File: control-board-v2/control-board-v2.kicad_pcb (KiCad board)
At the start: 2 copper layers, 90 x 50 mm, 134 parts, among them J1 Conn_01x03, J12 Conn_01x01_Pin, J13 Conn_01x01_Pin, J14 Conn_01x02, J15 Conn_01x01_Pin, J16 Conn_01x02, J17 Conn_01x02, J18 Conn_01x02, J19 Conn_01x01_Pin, J2 GPS_ANT, J20 Conn_01x01_Pin, J21 Conn_01x01_Pin, J22 Conn_01x01_Pin, J23 Conn_01x01_Pin, J24 Conn_01x01_Pin, J25 Conn_01x01_Pin, J26 Conn_01x01_Pin, J27 Conn_01x01_Pin, J28 Conn_01x01_Pin, J29 Conn_01x01_Pin, J3 Conn_01x01_Pin, J6 USB_C_Receptacle_USB2.0_16P, J7 Conn_01x01_Pin, U2 NEO-XM, U3 TCAN1462VDRQ1, U5 STM32H563RGTx, U6 AMS1117-3.3, U7 TCAN1462VDRQ1, U8 AP63200WU, Y1 25M

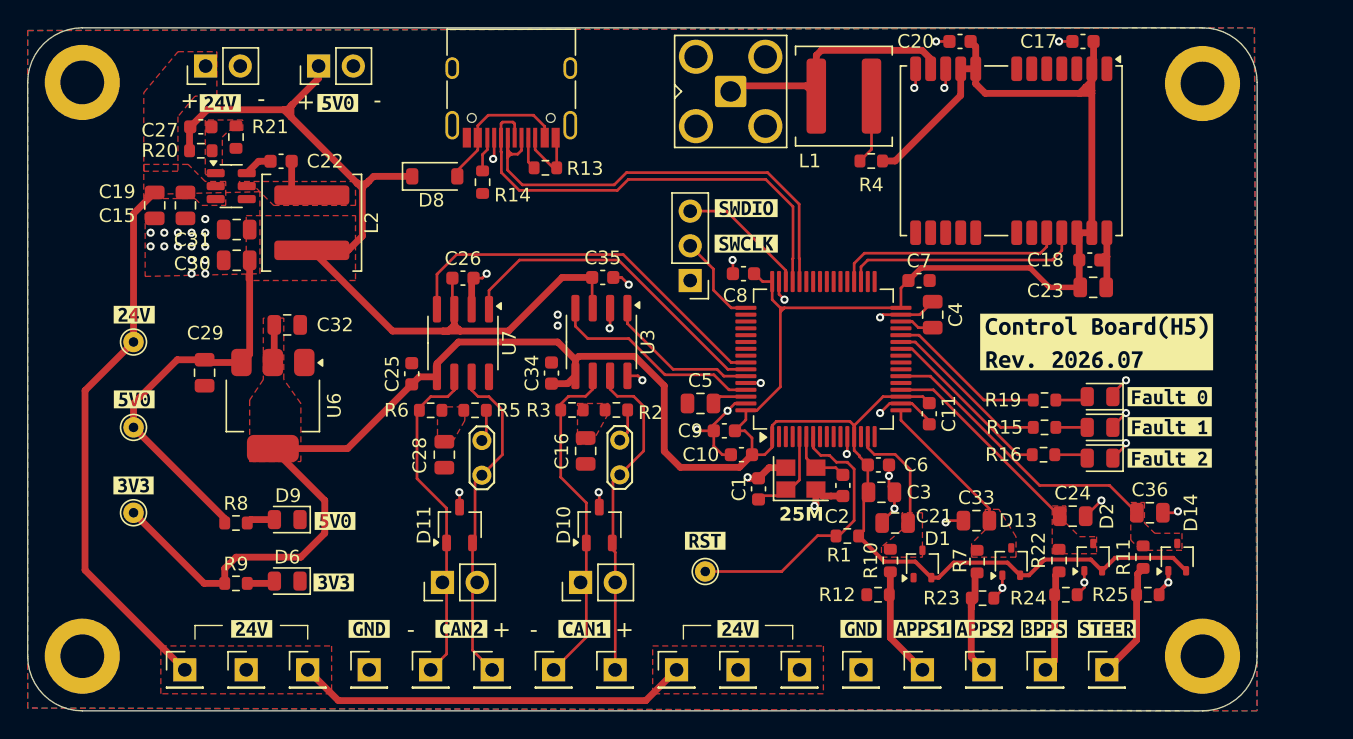
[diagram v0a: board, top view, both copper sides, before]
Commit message: feat: ctrl board-v2: add sd card, iso can
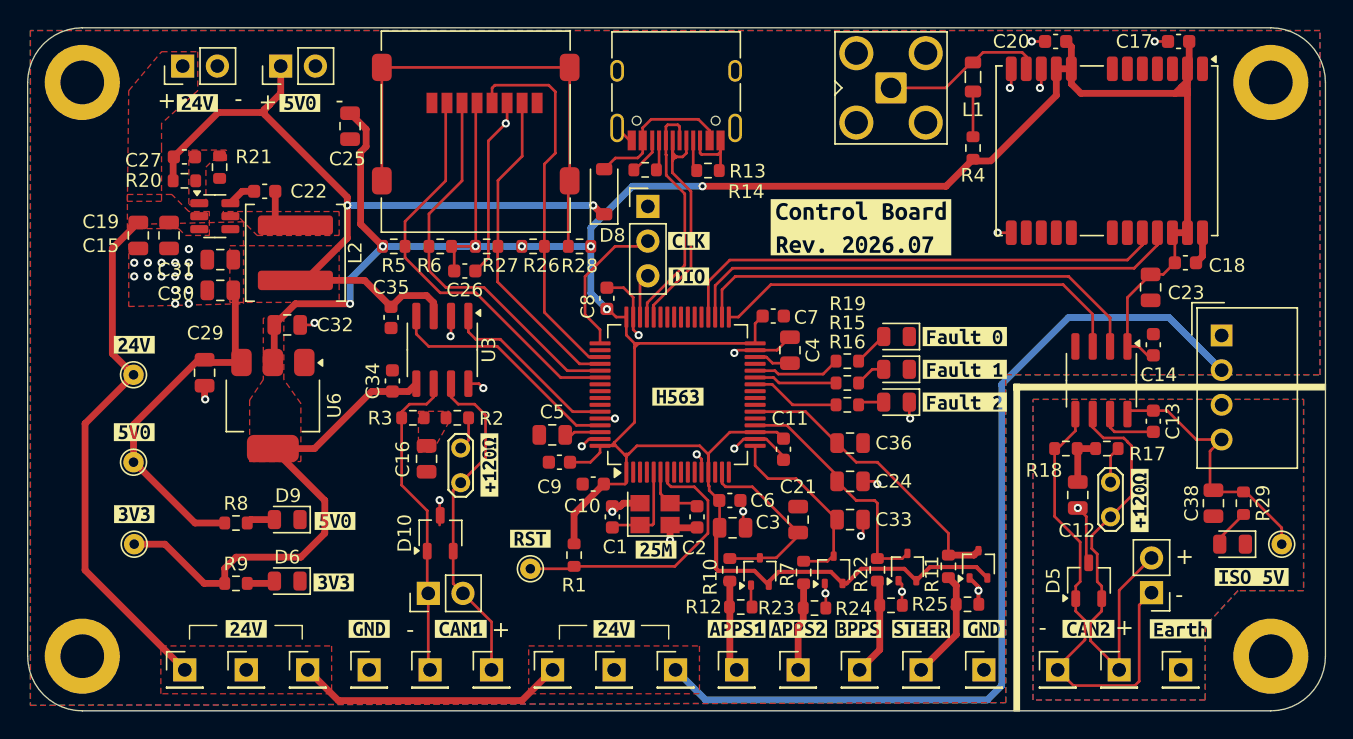
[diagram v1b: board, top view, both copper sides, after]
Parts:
- removed C28: 1u, Capacitor_SMD:C_0805_2012Metric
- removed D11: DESD2CAN2SOQ, Package_TO_SOT_SMD:TSOT-23
- removed JP2: Jumper_2_Open, TestPoint:TestPoint_2Pads_Pitch2.54mm_Drill0.8mm
- removed U7: TCAN1462VDRQ1, Package_SO:SOIC-8_3.9x4.9mm_P1.27mm
- removed kibuzzard-6A5650B6: G***, kibuzzard-6A5650B6
- removed kibuzzard-6A56A2DB: G***, kibuzzard-6A56A2DB
- removed kibuzzard-6A56A2EB: G***, kibuzzard-6A56A2EB
- added C12: 1u, Capacitor_SMD:C_0805_2012Metric, F.Cu at (177.9, 104.2)
- added C13: 100n, Capacitor_SMD:C_0603_1608Metric, F.Cu at (183.4, 98.8)
- added C14: 100n, Capacitor_SMD:C_0603_1608Metric, F.Cu at (183.4, 93.2)
- added C38: 10u, Capacitor_SMD:C_0805_2012Metric, F.Cu at (187.8, 104.8)
- added D5: DESD2CAN2SOQ, Package_TO_SOT_SMD:TSOT-23, F.Cu at (178.7, 110.5)
- added D7: LED, LED_SMD:LED_0805_2012Metric, F.Cu at (189.2, 107.8)
- added J4: Micro_SD_Card_Det1, microSD:microSD_HC_Molex_47219-2001, F.Cu at (133.8, 77.6)
- added J5: Conn_01x01_Pin, Connector_PinHeader_2.54mm:PinHeader_1x01_P2.54mm_Vertical, F.Cu at (185.4, 117.0)
- added JP3: Jumper_2_Open, TestPoint:TestPoint_2Pads_Pitch2.54mm_Drill0.8mm, F.Cu at (180.3, 105.8)
- added R17: 60R, Resistor_SMD:R_0603_1608Metric, F.Cu at (180.0, 100.8)
- added R18: 60R, Resistor_SMD:R_0603_1608Metric, F.Cu at (177.0, 100.8)
- added R26: 10k, Resistor_SMD:R_0603_1608Metric, F.Cu at (138.0, 86.0)
- added R27: 10k, Resistor_SMD:R_0603_1608Metric, F.Cu at (134.6, 86.0)
- added R28: 10k, Resistor_SMD:R_0603_1608Metric, F.Cu at (141.4, 86.0)
- added R29: 10k, Resistor_SMD:R_0603_1608Metric, F.Cu at (190.0, 104.8)
- added TP5: TP_iso5V, TestPoint:TestPoint_THTPad_D1.5mm_Drill0.7mm, F.Cu at (192.8, 107.8)
- added U1: ISO1042-Q1, Package_SO:SOIC-8_3.9x4.9mm_P1.27mm, F.Cu at (179.6, 95.8)
- added U4: SCT01F24S05, Converter_DCDC:Converter_DCDC_TRACO_TME_24xxS_Single_THT, F.Cu at (188.4, 92.5)
- added kibuzzard-6A57B3CB: G***, kibuzzard-6A57B3CB, F.Cu at (147.0, 108.2)
- added kibuzzard-6A57B602: G***, kibuzzard-6A57B602, F.Cu at (149.4, 88.2)
- added kibuzzard-6A57B60C: G***, kibuzzard-6A57B60C, F.Cu at (149.4, 85.6)
- added kibuzzard-6A57B8B6: G***, kibuzzard-6A57B8B6, F.Cu at (162.0, 84.6)
- added kibuzzard-6A57B8D1: G***, kibuzzard-6A57B8D1, F.Cu at (148.6, 97.0)
- added kibuzzard-6A57DAAA: G***, kibuzzard-6A57DAAA, F.Cu at (190.6, 110.2)
- added kibuzzard-6A57DE94: G***, kibuzzard-6A57DE94, F.Cu at (182.4, 104.6)
- added kibuzzard-6A57DE94: G***, kibuzzard-6A57DE94, F.Cu at (134.8, 102.0)
- added kibuzzard-6A58121F: G***, kibuzzard-6A58121F, F.Cu at (185.4, 114.0)
- C25: value 100n -> 1u; footprint Capacitor_SMD:C_0603_1608Metric -> Capacitor_SMD:C_0805_2012Metric
- L1: footprint Inductor_SMD:L_Coilcraft_XAL6060-XXX -> Inductor_SMD:L_0805_2012Metric
- R5, R6: value 60R -> 10k
- TP3: value TP_15V -> TP_24V
- moved J18 51.9 mm to (183.3, 111.3), turned to 180 degrees
- moved J22 45.9 mm to (180.9, 117.0)
- moved J23 45.9 mm to (176.4, 117.0)
- moved kibuzzard-6A569FE6 45.9 mm to (178.7, 114.0)
- moved C36 22.5 mm to (161.2, 100.4)
- moved R1 20.0 mm to (141.0, 108.6), turned to -90 degrees
- moved C25 18.7 mm to (124.6, 77.2), turned to -90 degrees
- moved C24 16.5 mm to (161.2, 103.2)
- moved C35 15.8 mm to (127.6, 91.2), turned to -90 degrees
- moved kibuzzard-6A5670B9 15.6 mm to (169.6, 92.6)
- moved kibuzzard-6A5670C2 15.6 mm to (169.6, 95.0)
- moved kibuzzard-6A5670CA 15.6 mm to (169.6, 97.4)
- moved D12 15.5 mm to (164.6, 92.6)
- moved D3 15.5 mm to (164.6, 95.0)
- moved D4 15.5 mm to (164.6, 97.4)
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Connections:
- net 15v renamed 24v
- C26 pad 1: +5V -> +3V3
- H3 pad 1: GND -> unconnected-(H3-Pad1)
- R5 pad 1: Net-(JP2-B) -> +3V3
- R5 pad 2: Net-(C28-Pad1) -> SD_CS
- R6 pad 1: Net-(C28-Pad1) -> +3V3
- R6 pad 2: CAN2_N -> SPI3_MOSI
- U5 pad 33: unconnected-(U5-PB12-Pad33) -> CAN2_RX
- U5 pad 34: unconnected-(U5-PB13-Pad34) -> CAN2_TX
- U5 pad 51: unconnected-(U5-PC10-Pad51) -> SPI3_SCK
- U5 pad 52: unconnected-(U5-PC11-Pad52) -> SPI3_MISO
- U5 pad 53: unconnected-(U5-PC12-Pad53) -> SPI3_MOSI
- U5 pad 54: unconnected-(U5-PD2-Pad54) -> SD_CS
- U5 pad 57: CAN2_RX -> unconnected-(U5-PB5-Pad57)
- U5 pad 58: CAN2_TX -> unconnected-(U5-PB6-Pad58)
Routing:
- net 24v: track 69.0 -> 125.5 mm
- net +3V3: track 218.1 -> 264.9 mm, vias 0 -> 7
- net Net-(J4-DET): track 0.00 -> 35.2 mm
- net SD_CS: track 0.00 -> 30.5 mm
- net SPI3_MOSI: track 0.00 -> 28.8 mm
- net SPI3_SCK: track 0.00 -> 27.9 mm
- net SPI3_MISO: track 0.00 -> 23.8 mm
- net +ISO5V: track 0.00 -> 19.6 mm
- net UART_GPS_RX: track 17.0 -> 36.4 mm
- net UART_GPS_TX: track 17.6 -> 36.8 mm
- net DN: track 35.1 -> 18.5 mm
- net DP: track 34.2 -> 17.8 mm
- net CAN2_N: track 24.7 -> 35.8 mm
- net CAN2_TX: track 24.4 -> 34.2 mm
- net Earth: track 0.00 -> 8.62 mm, vias 0 -> 1
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- added copper zone on B.Cu, net Earth
- added copper zone on F.Cu, net Earth
- removed copper zone on F.Cu, net ADC_APPS1
- removed copper zone on F.Cu, net ADC_APPS2
- removed copper zone on F.Cu, net ADC_BPPS
- removed copper zone on F.Cu, net ADC_STEER
- removed copper zone on F.Cu, net Net-(C28-Pad1)
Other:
- board size 90 x 50 mm -> 95 x 50 mm
- board text removed: "25M"

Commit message: feat: ctrl board: add logo
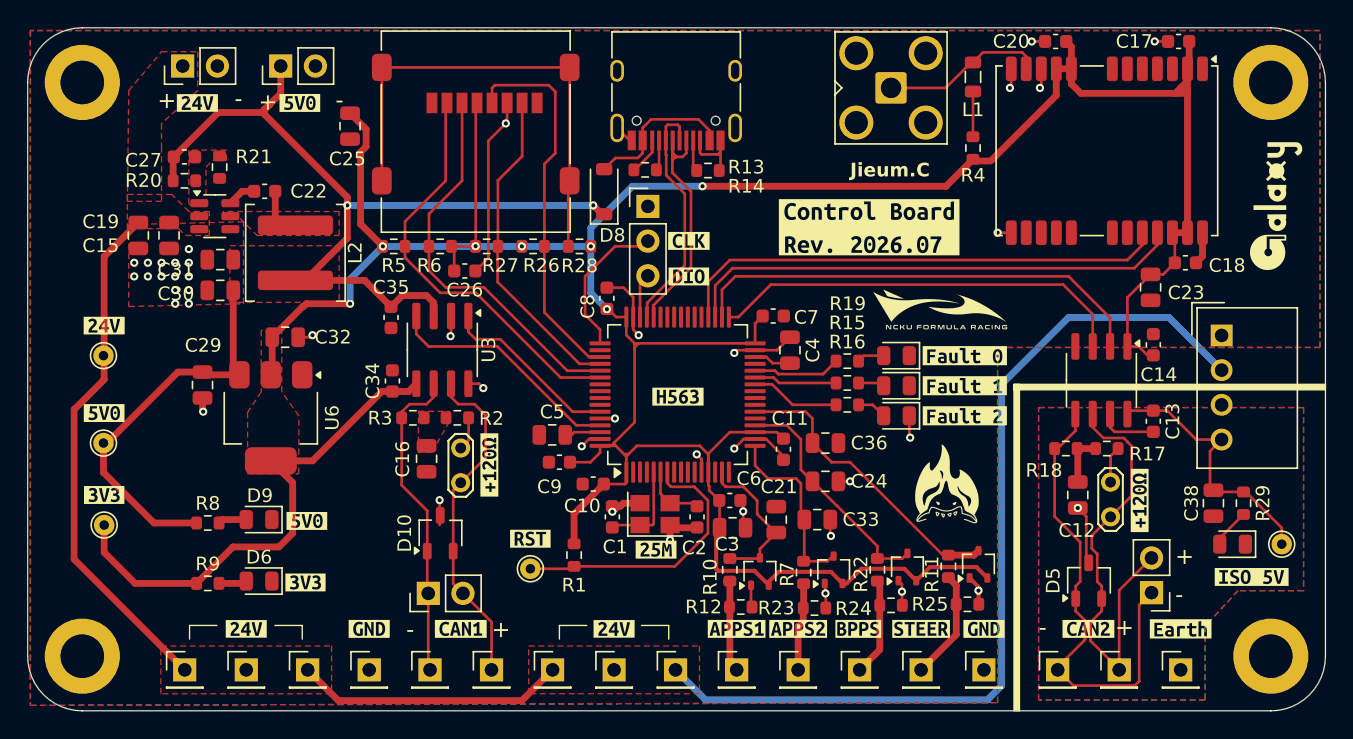
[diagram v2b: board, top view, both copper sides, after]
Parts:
- added G***: LOGO, Custom_logo:nckufs_logo_10mm, F.Cu at (167.8, 90.6)
- added G***: LOGO, Custom_logo:galaxy_logo_10mm, F.Cu at (192.4, 83.0)
- added G***: LOGO, Custom_logo:fire_shark_8mm, F.Cu at (168.4, 103.4)
- moved TP3 2.61 mm to (106.5, 94.0)
- moved kibuzzard-6A569F1D 2.61 mm to (106.6, 91.8)
- moved TP1 2.61 mm to (106.5, 100.4)
- moved TP2 2.61 mm to (106.6, 106.4)
- moved kibuzzard-6A56A219 2.61 mm to (106.6, 104.2)
- moved kibuzzard-6A56A32D 2.61 mm to (106.6, 98.2)
- moved C33 2.40 mm to (158.8, 106.0)
- moved D6 2.06 mm to (117.9, 110.5)
- moved D9 2.06 mm to (117.9, 106.0)
- moved R8 2.06 mm to (114.2, 106.2)
- moved R9 2.06 mm to (114.2, 110.7)
- moved kibuzzard-6A56A219 2.06 mm to (121.3, 110.6)
- moved kibuzzard-6A56A32D 2.06 mm to (121.4, 106.1)
- moved C24 1.80 mm to (159.4, 103.2)
- moved C36 1.80 mm to (159.4, 100.4)
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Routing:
- net +5V: track 89.2 -> 92.0 mm
- net ADC_APPS1: track 13.8 -> 11.4 mm
- net ADC_BPPS: track 18.0 -> 17.2 mm
- net ADC_APPS2: track 14.2 -> 13.5 mm
- net 24v: track 125.5 -> 124.8 mm
- net Net-(D12-A): track 2.58 -> 2.00 mm
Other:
- board text added: "Jieum.C"

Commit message: modify layout
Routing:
- net +3V3: track 265.1 -> 267.8 mm
- net +5V: track 92.0 -> 92.9 mm
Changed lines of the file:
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@@
+	)
+	(segment
+		(start 185.9 74.8)
+		(end 185.9 75.4)
+		(width 0.5)
+		(layer "F.Cu")
+		(net 4)
 	)
 	(segment
@@
 	)
 	(segment
+		(start 150.826304 101.173696)
+		(end 151 101)
+		(width 0.2)
+		(layer "F.Cu")
+		(net 4)
+	)
+	(segment
 		(start 116.0325 108)
 		(end 119.4 108)
@@
 	)
 	(segment
+		(start 145.2 101)
+		(end 145.6 100.6)
+		(width 0.2)
+		(layer "F.Cu")
+		(net 4)
+	)
+	(segment
 		(start 145.6 100.6)
 		(end 150.2 100.6)
@@
 	)
 	(segment
-		(start 143.954357 100.354357)
-		(end 145.426304 98.88241)
-		(width 0.2)
-		(layer "F.Cu")
-		(net 4)
-	)
-	(segment
 		(start 144.826304 101.373696)
 		(end 145 101.2)
@@
 	)
 	(segment
-		(start 150.826304 101.173696)
-		(end 152.4 99.6)
-		(width 0.2)
-		(layer "F.Cu")
-		(net 4)
-	)
-	(segment
 		(start 159.799674 109.825)
 		(end 160.649674 110.675)
@@
 	)
 	(segment
+		(start 144.526304 101.073696)
+		(end 145.126304 101.073696)
+		(width 0.2)
+		(layer "F.Cu")
+		(net 4)
+	)
+	(segment
 		(start 184.8 85)
 		(end 185.9 85)
@@
 	)
 	(segment
-		(start 150.2 100.6)
-		(end 150.826304 101.226304)
-		(width 0.2)
-		(layer "F.Cu")
-		(net 4)
-	)
-	(segment
 		(start 185.9 73.9)
 		(end 185.9 73)
@@
 	)
 	(segment
+		(start 143.954357 100.354357)
+		(end 144.154357 100.154357)
+		(width 0.2)
+		(layer "F.Cu")
+		(net 4)
+	)
+	(segment
 		(start 133.8 75.595)
 		(end 133.8 85.975)
@@
 	)
 	(segment
+		(start 150.6 101)
+		(end 150.826304 101.226304)
+		(width 0.2)
+		(layer "F.Cu")
+		(net 4)
+	)
+	(segment
 		(start 177.4 71.375)
 		(end 177.025 71)
@@
 	)
 	(segment
+		(start 145.126304 101.073696)
+		(end 145.2 101)
+		(width 0.2)
+		(layer "F.Cu")
+		(net 4)
+	)
+	(segment
 		(start 150.826304 101.545643)
 		(end 150.826304 101.173696)
@@
 	)
 	(segment
+		(start 150.2 100.6)
+		(end 150.6 101)
+		(width 0.2)
+		(layer "F.Cu")
+		(net 4)
+	)
+	(segment
 		(start 185 74.8)
 		(end 185.45 74.35)
@@
 	)
 	(segment
+		(start 185.9 75.4)
+		(end 185.9 85)
+		(width 0.5)
+		(layer "F.Cu")
+		(net 4)
+	)
+	(segment
 		(start 183.2 88.05)
 		(end 184.125 88.05)
@@
 	)
 	(segment
+		(start 144.154357 100.154357)
+		(end 145.426304 98.88241)
+		(width 0.2)
+		(layer "F.Cu")
+		(net 4)
+	)
+	(segment
 		(start 121.4 90.2)
 		(end 124.6 90.2)
@@
 	)
 	(segment
-		(start 144.006965 100.554357)
-		(end 144.726304 101.273696)
-		(width 0.2)
-		(layer "F.Cu")
-		(net 4)
-	)
-	(segment
 		(start 160.950326 110.675)
 		(end 162.025326 109.6)
@@
 	)
 	(segment
+		(start 185 74.8)
+		(end 185.3 74.8)
+		(width 0.5)
+		(layer "F.Cu")
+		(net 4)
+	)
+	(segment
 		(start 126.925 96.625)
 		(end 127.7 96.625)
@@
 	)
 	(segment
-		(start 145 101.2)
-		(end 145.6 100.6)
-		(width 0.2)
-		(layer "F.Cu")
-		(net 4)
-	)
-	(segment
 		(start 144.726304 101.273696)
 		(end 144.826304 101.373696)
@@
 	)
 	(segment
+		(start 144.006965 100.301749)
+		(end 144.006965 100.554357)
+		(width 0.2)
+		(layer "F.Cu")
+		(net 4)
+	)
+	(segment
 		(start 177.4 73)
 		(end 177.4 74.1)
@@
 	)
 	(segment
+		(start 151 101)
+		(end 152.4 99.6)
+		(width 0.2)
+		(layer "F.Cu")
+		(net 4)
+	)
+	(segment
 		(start 113.3625 110.67)
 		(end 108.87 110.67)
@@
 	)
 	(segment
+		(start 144.526304 101.073696)
+		(end 144.726304 101.273696)
+		(width 0.2)
+		(layer "F.Cu")
+		(net 4)
+	)
+	(segment
+		(start 185.3 74.8)
+		(end 185.9 75.4)
+		(width 0.5)
+		(layer "F.Cu")
+		(net 4)
+	)
+	(segment
 		(start 181.505 93.325)
 		(end 182.325 93.325)
@@
 	)
 	(segment
+		(start 144.154357 100.154357)
+		(end 144.006965 100.301749)
+		(width 0.2)
+		(layer "F.Cu")
+		(net 4)
+	)
+	(segment
 		(start 141 107.775)
 		(end 141 105.575)
@@
 	)
 	(segment
+		(start 150.6 101)
+		(end 151 101)
+		(width 0.2)
+		(layer "F.Cu")
+		(net 4)
+	)
+	(segment
 		(start 165.174674 109.6)
 		(end 166.049674 110.475)
@@
 	)
 	(segment
-		(start 185.9 74.8)
-		(end 185.9 85)
-		(width 0.5)
-		(layer "F.Cu")
-		(net 4)
-	)
-	(segment
 		(start 118.8 101.7)
 		(end 121.85 101.7)
@@
 	)
 	(segment
+		(start 145 101.2)
+		(end 145.2 101)
+		(width 0.2)
+		(layer "F.Cu")
+		(net 4)
+	)
+	(segment
 		(start 185.9 74.6)
 		(end 185.9 74.8)
@@
 		(end 129.45 96.05)
 		(width 0.5)
+		(layer "F.Cu")
+		(net 4)
+	)
+	(segment
+		(start 144.006965 100.554357)
+		(end 144.526304 101.073696)
+		(width 0.2)
 		(layer "F.Cu")
 		(net 4)
@@
 	)
 	(segment
+		(start 118.6 75.725)
+		(end 118.6 76.6)
+		(width 0.5)
+		(layer "F.Cu")
+		(net 9)
+	)
+	(segment
 		(start 118.125 76.2)
 		(end 114.95 76.2)
@@
 	)
 	(segment
+		(start 118.725 75.6)
+		(end 118.6 75.725)
+		(width 0.5)
+		(layer "F.Cu")
+		(net 9)
+	)
+	(segment
 		(start 130.2 89.6)
 		(end 130.72 90.12)
@@
 	)
 	(segment
+		(start 124.4 82.4)
+		(end 118.6 76.6)
+		(width 0.5)
+		(layer "F.Cu")
+		(net 9)
+	)
+	(segment
 		(start 124.4 85.4)
 		(end 124.4 83)
@@
 	)
 	(segment
-		(start 124.4 82.4)
-		(end 118.325 76.325)
-		(width 0.5)
-		(layer "F.Cu")
-		(net 9)
-	)
-	(segment
 		(start 116.05 94.95)
 		(end 116.05 89.22)
@@
 	)
 	(segment
+		(start 118.6 76.6)
+		(end 118.325 76.325)
+		(width 0.5)
+		(layer "F.Cu")
+		(net 9)
+	)
+	(segment
 		(start 106.55 100.65)
 		(end 106.55 102.55)
@@
 		(width 0.5)
 		(layer "F.Cu")
-		(net 9)
-	)
-	(segment
-		(start 118.725 75.6)
-		(end 118.6 75.725)
-		(width 0.5)
-		(layer "F.Cu")

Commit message: fix: schottky diode
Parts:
- removed D13, D14, D2: BAT54SW, Package_TO_SOT_SMD:SOT-323_SC-70
- removed the G*** at (168.4, 103.4)
- added D11: BAT46W-7-F, BAT46W-7-F:SOD3715X145N, F.Cu at (152.2, 110.9)
- added D15: BAT46W-7-F, BAT46W-7-F:SOD3715X145N, F.Cu at (168.0, 110.2)
- added D16: BAT46W-7-F, BAT46W-7-F:SOD3715X145N, F.Cu at (170.8, 103.5)
- added D17: BAT46W-7-F, BAT46W-7-F:SOD3715X145N, F.Cu at (168.0, 103.5)
- added D18: BAT46W-7-F, BAT46W-7-F:SOD3715X145N, F.Cu at (155.0, 110.9)
- added D19: BAT46W-7-F, BAT46W-7-F:SOD3715X145N, F.Cu at (164.0, 110.2)
- added D20: BAT46W-7-F, BAT46W-7-F:SOD3715X145N, F.Cu at (161.2, 110.2)
- D1: value BAT54SW -> BAT46W-7-F; footprint Package_TO_SOT_SMD:SOT-323_SC-70 -> BAT46W-7-F:SOD3715X145N
- moved D1 16.2 mm to (170.8, 110.2)
- moved R25 9.76 mm to (164.9, 103.8)
- moved R11 8.62 mm to (165.0, 101.5), turned to 180 degrees
- moved R22 4.09 mm to (165.0, 106.0), turned to 0 degrees
- moved R12 3.91 mm to (149.3, 112.7)
- moved R24 3.31 mm to (166.0, 109.5), turned to -90 degrees
- moved R10 2.91 mm to (149.5, 109.9)
- moved R7 0.94 mm to (158.5, 109.2)
- moved R23 0.69 mm to (158.3, 111.8)
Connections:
- D1 pad 1: GND -> +3V3
- D1 pad 2: +3V3 -> ADC_BPPS
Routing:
- net 24v: track 124.8 -> 143.6 mm
- net +5V: track 92.9 -> 105.2 mm
- net GND: track 74.0 -> 62.7 mm, vias 41 -> 35
- net STEER_in: track 8.33 -> 18.7 mm, vias 0 -> 1
- net BPPS_in: track 7.22 -> 15.4 mm, vias 0 -> 1
- net +3V3: track 267.8 -> 274.0 mm, vias 7 -> 9
- net Net-(U8-FB): track 0.00 -> 5.35 mm
- net Net-(U8-SW): track 3.95 -> 8.99 mm
- net ADC_BPPS: track 17.2 -> 21.9 mm
- net ADC_APPS1: track 11.4 -> 15.1 mm
- net APPS2_in: track 6.47 -> 9.69 mm, vias 0 -> 1
- net ADC_APPS2: track 13.5 -> 16.3 mm
- net ADC_STEER: track 21.9 -> 19.7 mm
- net APPS1_in: track 6.97 -> 8.55 mm
